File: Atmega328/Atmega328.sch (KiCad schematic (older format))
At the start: 30 parts, among them J1 Conn_01x02, J2 Conn_02x03_Odd_Even, J3 Conn_01x14, SW1 SW_Push, U1 LM358, U2 LM358, U3 LM78M05_TO252, U4 ATmega328P-PU, U5 DHT11, Y1 12MHz

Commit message: Fix footprints
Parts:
- J3: footprint Connector_PinSocket_1.27mm:PinSocket_1x14_P1.27mm_Vertical -> Connector_PinSocket_2.54mm:PinSocket_1x14_P2.54mm_Vertical
- U1, U2: footprint Package_SO:VSSOP-8_3.0x3.0mm_P0.65mm -> Package_SO:SOIC-8_3.9x4.9mm_P1.27mm
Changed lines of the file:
@@
 F 0 "U1" H 1900 2917 50  0000 C CNN
 F 1 "LM358" H 1900 2826 50  0000 C CNN
-F 2 "Package_SO:VSSOP-8_3.0x3.0mm_P0.65mm" H 1900 2550 50  0001 C CNN
+F 2 "Package_SO:SOIC-8_3.9x4.9mm_P1.27mm" H 1900 2550 50  0001 C CNN
 F 3 "http://www.ti.com/lit/ds/symlink/lm2904-n.pdf" H 1900 2550 50  0001 C CNN
 	1    1900 2550
@@
 F 0 "U1" H 1108 3146 50  0000 L CNN
 F 1 "LM358" H 1108 3055 50  0000 L CNN
-F 2 "Package_SO:VSSOP-8_3.0x3.0mm_P0.65mm" H 1150 3100 50  0001 C CNN
+F 2 "Package_SO:SOIC-8_3.9x4.9mm_P1.27mm" H 1150 3100 50  0001 C CNN
 F 3 "http://www.ti.com/lit/ds/symlink/lm2904-n.pdf" H 1150 3100 50  0001 C CNN
 	3    1150 3100
@@
 F 0 "U2" H 1108 4596 50  0000 L CNN
 F 1 "LM358" H 1108 4505 50  0000 L CNN
-F 2 "Package_SO:VSSOP-8_3.0x3.0mm_P0.65mm" H 1150 4550 50  0001 C CNN
+F 2 "Package_SO:SOIC-8_3.9x4.9mm_P1.27mm" H 1150 4550 50  0001 C CNN
 F 3 "http://www.ti.com/lit/ds/symlink/lm2904-n.pdf" H 1150 4550 50  0001 C CNN
 	3    1150 4550
@@
 F 0 "U2" H 2150 5217 50  0000 C CNN
 F 1 "LM358" H 2150 5126 50  0000 C CNN
-F 2 "Package_SO:VSSOP-8_3.0x3.0mm_P0.65mm" H 2150 4850 50  0001 C CNN
+F 2 "Package_SO:SOIC-8_3.9x4.9mm_P1.27mm" H 2150 4850 50  0001 C CNN
 F 3 "http://www.ti.com/lit/ds/symlink/lm2904-n.pdf" H 2150 4850 50  0001 C CNN
 	1    2150 4850
@@
 F 0 "U1" H 3800 5267 50  0000 C CNN
 F 1 "LM358" H 3800 5176 50  0000 C CNN
-F 2 "Package_SO:VSSOP-8_3.0x3.0mm_P0.65mm" H 3800 4900 50  0001 C CNN
+F 2 "Package_SO:SOIC-8_3.9x4.9mm_P1.27mm" H 3800 4900 50  0001 C CNN
 F 3 "http://www.ti.com/lit/ds/symlink/lm2904-n.pdf" H 3800 4900 50  0001 C CNN
 	2    3800 4900
@@
 F 0 "J3" H 10580 3492 50  0000 L CNN
 F 1 "Conn_01x14" H 10580 3401 50  0000 L CNN
-F 2 "Connector_PinSocket_1.27mm:PinSocket_1x14_P1.27mm_Vertical" H 10500 3500 50  0001 C CNN
+F 2 "Connector_PinSocket_2.54mm:PinSocket_1x14_P2.54mm_Vertical" H 10500 3500 50  0001 C CNN
 F 3 "~" H 10500 3500 50  0001 C CNN
 	1    10500 3500

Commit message: PCB Cleanup and Ready
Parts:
- D1: footprint Diode_THT:D_DO-41_SOD81_P10.16mm_Horizontal -> Diode_THT:D_DO-34_SOD68_P7.62mm_Horizontal
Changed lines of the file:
@@
 F 0 "D1" H 1250 6084 50  0000 C CNN
 F 1 "1N5817" H 1250 6175 50  0000 C CNN
-F 2 "Diode_THT:D_DO-41_SOD81_P10.16mm_Horizontal" H 1250 6125 50  0001 C CNN
+F 2 "Diode_THT:D_DO-34_SOD68_P7.62mm_Horizontal" H 1250 6125 50  0001 C CNN
 F 3 "http://www.vishay.com/docs/88525/1n5817.pdf" H 1250 6300 50  0001 C CNN
 	1    1250 6300

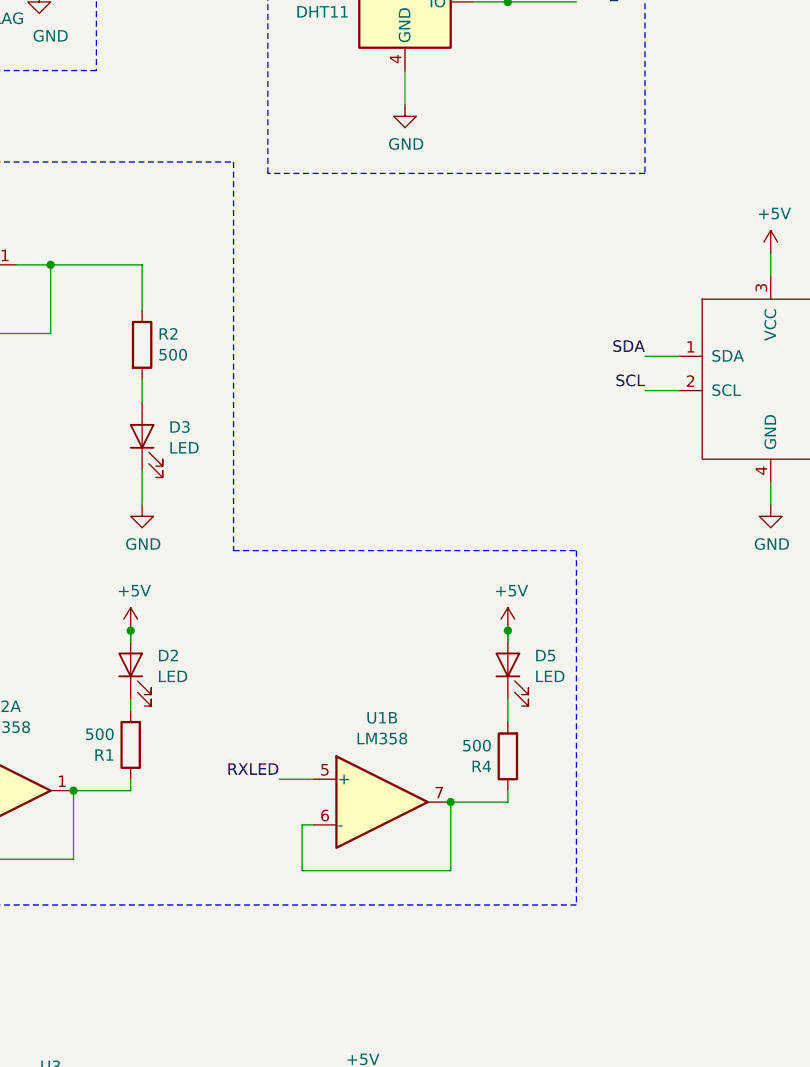
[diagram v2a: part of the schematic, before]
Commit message: Debug using OLED
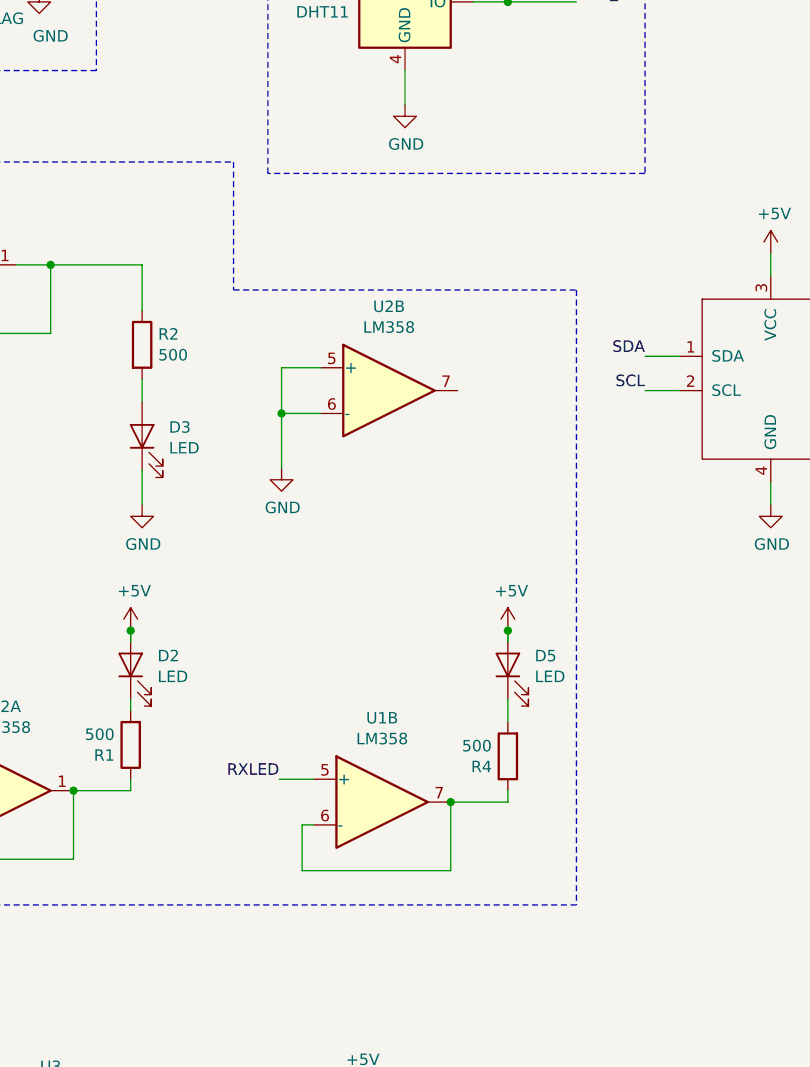
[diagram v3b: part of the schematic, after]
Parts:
- added unit 2 of U2
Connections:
- net GND: now also U2.5 (+), U2.6 (-)
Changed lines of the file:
@@
 	8950 2750 8700 2750
-Wire Notes Line
-	3150 2100 3150 3800
-Wire Notes Line
-	3150 3800 4650 3800
-Wire Notes Line
-	4650 3800 4650 5350
 Wire Notes Line
 	4650 5350 550  5350
@@
 Wire Wire Line
 	10250 4200 10300 4200
+$Comp
+L Amplifier_Operational:LM358 U2
+U 2 1 5D7B803A
+P 3830 3100
+F 0 "U2" H 3830 3467 50  0000 C CNN
+F 1 "LM358" H 3830 3376 50  0000 C CNN
+F 2 "" H 3830 3100 50  0001 C CNN
+F 3 "http://www.ti.com/lit/ds/symlink/lm2904-n.pdf" H 3830 3100 50  0001 C CNN
+	2    3830 3100
+	1    0    0    -1
+$EndComp
+Wire Wire Line
+	3530 3000 3360 3000
+Wire Wire Line
+	3360 3000 3360 3200
+Wire Wire Line
+	3530 3200 3360 3200
+Connection ~ 3360 3200
+Wire Wire Line
+	3360 3200 3360 3440
+$Comp
+L power:GND #PWR024
+U 1 1 5D7D0E9D
+P 3360 3440
+F 0 "#PWR024" H 3360 3190 50  0001 C CNN
+F 1 "GND" H 3365 3267 50  0000 C CNN
+F 2 "" H 3360 3440 50  0001 C CNN
+F 3 "" H 3360 3440 50  0001 C CNN
+	1    3360 3440
+	1    0    0    -1
+$EndComp
+Wire Notes Line
+	3150 2100 3150 2660
+Wire Notes Line
+	3150 2660 4650 2660
+Wire Notes Line
+	4650 2660 4650 5350
 $EndSCHEMATC
